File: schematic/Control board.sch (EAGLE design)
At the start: 14 parts, among them IC2 ATTINY44A

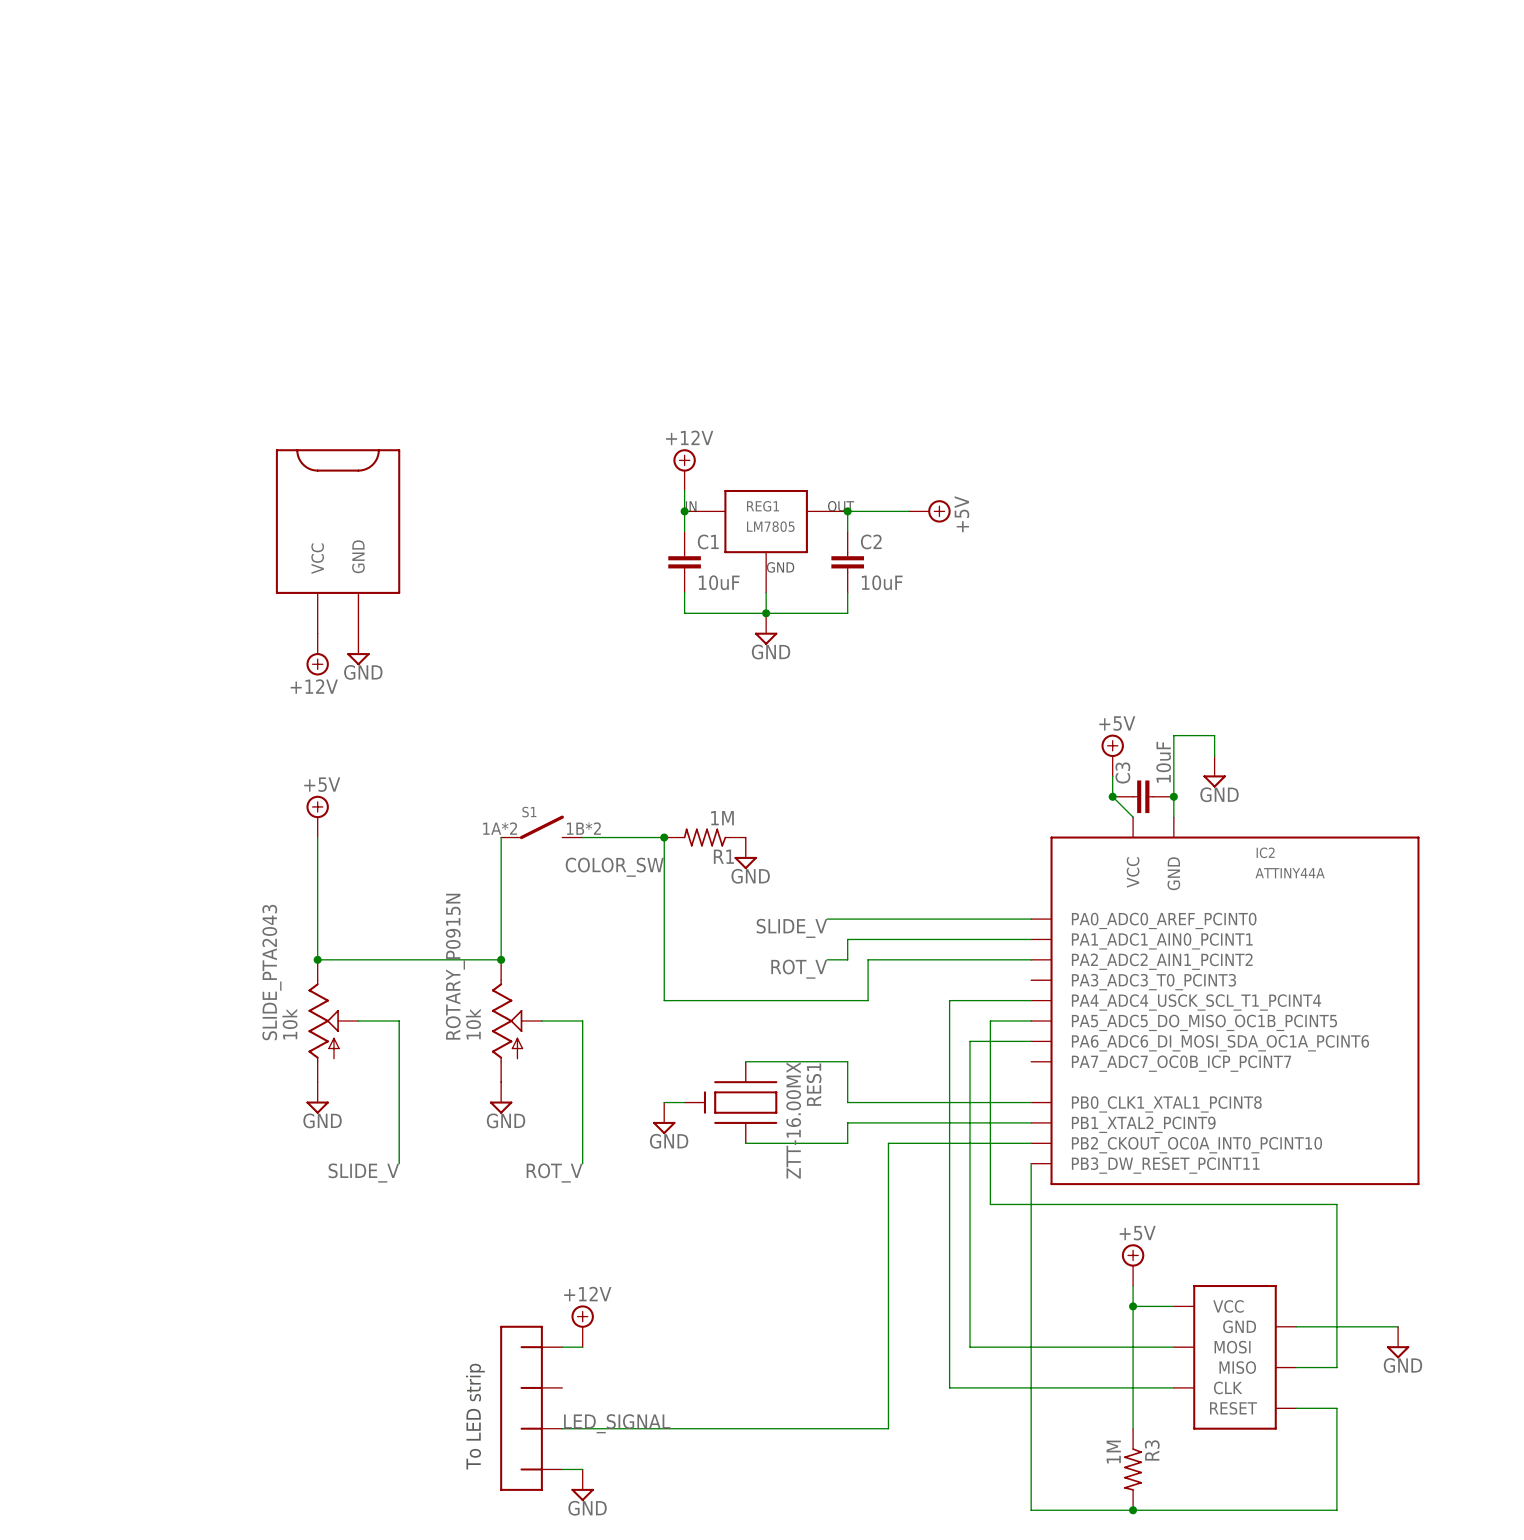
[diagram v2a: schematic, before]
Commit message: Voltage regulator and DIP microcontroller are too big, replacing with small SMD components
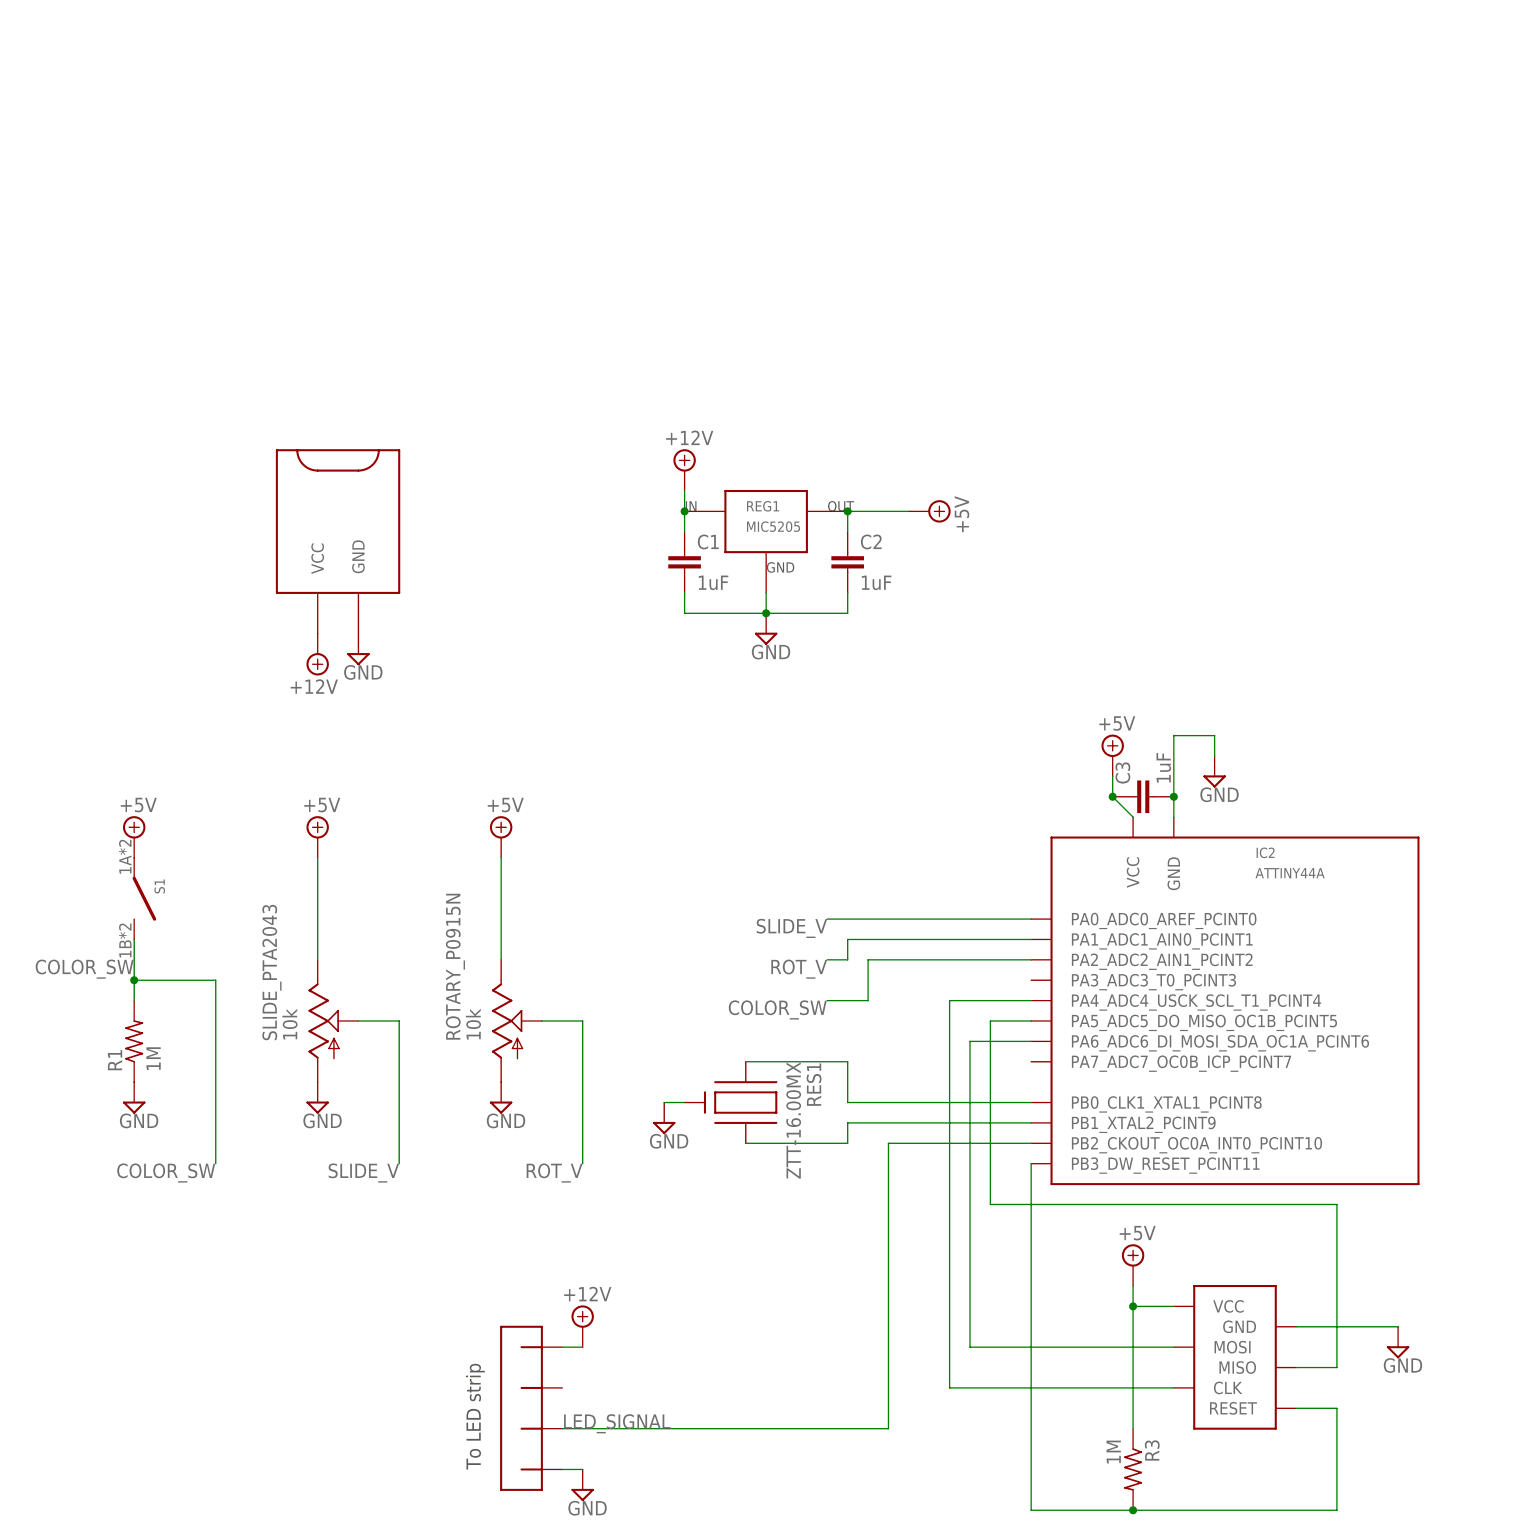
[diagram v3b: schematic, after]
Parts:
- C1, C2, C3: value 10uF -> 1uF
- REG1: value LM7805 -> MIC5205; device RGB LED project:LM7805 -> RGB LED project:MIC5205
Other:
- moved on the sheet: R1, S1
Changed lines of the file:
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@@
 <part name="SUPPLY4" library="supply2" deviceset="GND" device=""/>
 <part name="SUPPLY5" library="supply2" deviceset="+12V" device=""/>
-<part name="C1" library="resistor" deviceset="C-EU" device="C0603" value="10uF"/>
+<part name="C1" library="resistor" deviceset="C-EU" device="C0603" value="1uF"/>
 <part name="SUPPLY6" library="supply2" deviceset="GND" device=""/>
 <part name="SUPPLY8" library="supply2" deviceset="+5V" device=""/>
@@
 <part name="SUPPLY17" library="supply2" deviceset="GND" device=""/>
 <part name="CONN1" library="RGB LED project" deviceset="4-PIN-RIGHT-ANGLE" device=""/>
-<part name="REG1" library="RGB LED project" deviceset="LM7805" device="" value="LM7805"/>
-<part name="C2" library="resistor" deviceset="C-EU" device="C0603" value="10uF"/>
-<part name="C3" library="resistor" deviceset="C-EU" device="C0603" value="10uF"/>
+<part name="C2" library="resistor" deviceset="C-EU" device="C0603" value="1uF"/>
+<part name="C3" library="resistor" deviceset="C-EU" device="C0603" value="1uF"/>
+<part name="REG1" library="RGB LED project" deviceset="MIC5205" device=""/>
+<part name="SUPPLY7" library="supply2" deviceset="+5V" device=""/>
+<part name="SUPPLY18" library="supply2" deviceset="+5V" device=""/>
 </parts>
 <sheets>
@@
 </plain>
 <instances>
-<instance part="S1" gate="G$1" x="-35.56" y="-7.62"/>
+<instance part="S1" gate="G$1" x="-83.82" y="-12.7" rot="R270"/>
 <instance part="ROTARY_P0915N" gate="G$1" x="-38.1" y="-30.48"/>
 <instance part="SLIDE_PTA2043" gate="G$1" x="-60.96" y="-30.48"/>
-<instance part="SUPPLY1" gate="+5V" x="-60.96" y="-5.08"/>
+<instance part="SUPPLY1" gate="+5V" x="-60.96" y="-7.62"/>
 <instance part="SUPPLY2" gate="GND" x="-60.96" y="-40.64"/>
 <instance part="SUPPLY3" gate="GND" x="-38.1" y="-40.64"/>
-<instance part="R1" gate="G$1" x="-12.7" y="-7.62" rot="R180"/>
-<instance part="SUPPLY4" gate="GND" x="-7.62" y="-10.16"/>
+<instance part="R1" gate="G$1" x="-83.82" y="-33.02" rot="R90"/>
+<instance part="SUPPLY4" gate="GND" x="-83.82" y="-40.64"/>
 <instance part="SUPPLY5" gate="+12V" x="-15.24" y="38.1"/>
 <instance part="C1" gate="G$1" x="-15.24" y="27.94"/>
@@
 <instance part="SUPPLY17" gate="GND" x="-27.94" y="-88.9"/>
 <instance part="CONN1" gate="G$1" x="-35.56" y="-78.74" rot="R180"/>
-<instance part="REG1" gate="G$1" x="-5.08" y="33.02"/>
 <instance part="C2" gate="G$1" x="5.08" y="27.94"/>
 <instance part="C3" gate="G$1" x="40.64" y="-2.54" rot="R90"/>
+<instance part="REG1" gate="G$1" x="-5.08" y="33.02"/>
+<instance part="SUPPLY7" gate="+5V" x="-38.1" y="-7.62"/>
+<instance part="SUPPLY18" gate="+5V" x="-83.82" y="-7.62"/>
 </instances>
 <busses>
@@
 <pinref part="SUPPLY1" gate="+5V" pin="+5V"/>
 <pinref part="SLIDE_PTA2043" gate="G$1" pin="B"/>
-<wire x1="-60.96" y1="-7.62" x2="-60.96" y2="-22.86" width="0.1524" layer="91"/>
-<pinref part="ROTARY_P0915N" gate="G$1" pin="B"/>
-<wire x1="-60.96" y1="-22.86" x2="-38.1" y2="-22.86" width="0.1524" layer="91"/>
-<pinref part="S1" gate="G$1" pin="P$1"/>
-<wire x1="-38.1" y1="-22.86" x2="-38.1" y2="-7.62" width="0.1524" layer="91"/>
-<junction x="-60.96" y="-22.86"/>
-<junction x="-38.1" y="-22.86"/>
+<wire x1="-60.96" y1="-10.16" x2="-60.96" y2="-22.86" width="0.1524" layer="91"/>
 </segment>
 <segment>
 <wire x1="5.08" y1="33.02" x2="12.7" y2="33.02" width="0.1524" layer="91"/>
 <pinref part="SUPPLY8" gate="+5V" pin="+5V"/>
-<pinref part="REG1" gate="G$1" pin="OUT"/>
 <pinref part="C2" gate="G$1" pin="1"/>
 <wire x1="5.08" y1="30.48" x2="5.08" y2="33.02" width="0.1524" layer="91"/>
+<pinref part="REG1" gate="G$1" pin="OUT"/>
 <junction x="5.08" y="33.02"/>
 </segment>
@@
 <junction x="40.64" y="-66.04"/>
 </segment>
+<segment>
+<pinref part="S1" gate="G$1" pin="P$1"/>
+<pinref part="SUPPLY18" gate="+5V" pin="+5V"/>
+</segment>
+<segment>
+<pinref part="ROTARY_P0915N" gate="G$1" pin="B"/>
+<pinref part="SUPPLY7" gate="+5V" pin="+5V"/>
+<wire x1="-38.1" y1="-10.16" x2="-38.1" y2="-22.86" width="0.1524" layer="91"/>
+</segment>
 </net>
 <net name="SLIDE_V" class="0">
@@
 <net name="COLOR_SW" class="0">
 <segment>
-<pinref part="S1" gate="G$1" pin="P$2"/>
-<wire x1="-27.94" y1="-7.62" x2="-17.78" y2="-7.62" width="0.1524" layer="91"/>
-<wire x1="-17.78" y1="-7.62" x2="-17.78" y2="-27.94" width="0.1524" layer="91"/>
-<pinref part="R1" gate="G$1" pin="2"/>
-<junction x="-17.78" y="-7.62"/>
-<label x="-17.78" y="-10.16" size="1.778" layer="95" rot="R180"/>
+<label x="-83.82" y="-22.86" size="1.778" layer="95" rot="R180"/>
 <pinref part="IC2" gate="G$1" pin="PA2_ADC2_AIN1_PCINT2"/>
 <wire x1="27.94" y1="-22.86" x2="7.62" y2="-22.86" width="0.1524" layer="91"/>
 <wire x1="7.62" y1="-22.86" x2="7.62" y2="-27.94" width="0.1524" layer="91"/>
-<wire x1="7.62" y1="-27.94" x2="-17.78" y2="-27.94" width="0.1524" layer="91"/>
+<label x="2.54" y="-27.94" size="1.778" layer="95" rot="R180"/>
+<wire x1="7.62" y1="-27.94" x2="2.54" y2="-27.94" width="0.1524" layer="91"/>
+</segment>
+<segment>
+<pinref part="S1" gate="G$1" pin="P$2"/>
+<pinref part="R1" gate="G$1" pin="2"/>
+<wire x1="-83.82" y1="-27.94" x2="-83.82" y2="-25.4" width="0.1524" layer="91"/>
+<wire x1="-83.82" y1="-25.4" x2="-83.82" y2="-20.32" width="0.1524" layer="91"/>
+<wire x1="-83.82" y1="-25.4" x2="-73.66" y2="-25.4" width="0.1524" layer="91"/>
+<wire x1="-73.66" y1="-25.4" x2="-73.66" y2="-48.26" width="0.1524" layer="91"/>
+<junction x="-83.82" y="-25.4"/>
+<label x="-73.66" y="-48.26" size="1.778" layer="95" rot="R180"/>
 </segment>
 </net>
@@
 <pinref part="SUPPLY6" gate="GND" pin="GND"/>
 <junction x="-5.08" y="20.32"/>
-<pinref part="REG1" gate="G$1" pin="GND"/>
 <pinref part="C2" gate="G$1" pin="2"/>
 <wire x1="-5.08" y1="20.32" x2="5.08" y2="20.32" width="0.1524" layer="91"/>
 <wire x1="5.08" y1="20.32" x2="5.08" y2="22.86" width="0.1524" layer="91"/>
+<pinref part="REG1" gate="G$1" pin="GND"/>
 </segment>
 <segment>
@@
 <segment>
 <pinref part="SUPPLY5" gate="+12V" pin="+12V"/>
-<wire x1="-15.24" y1="35.56" x2="-15.24" y2="33.02" width="0.1524" layer="91"/>
 <pinref part="C1" gate="G$1" pin="1"/>
 <wire x1="-15.24" y1="30.48" x2="-15.24" y2="33.02" width="0.1524" layer="91"/>
+<pinref part="REG1" gate="G$1" pin="IN"/>
+<wire x1="-15.24" y1="33.02" x2="-15.24" y2="35.56" width="0.1524" layer="91"/>
 <junction x="-15.24" y="33.02"/>
-<pinref part="REG1" gate="G$1" pin="IN"/>
-</segment>
-<segment>
+</segment>
+<segment>

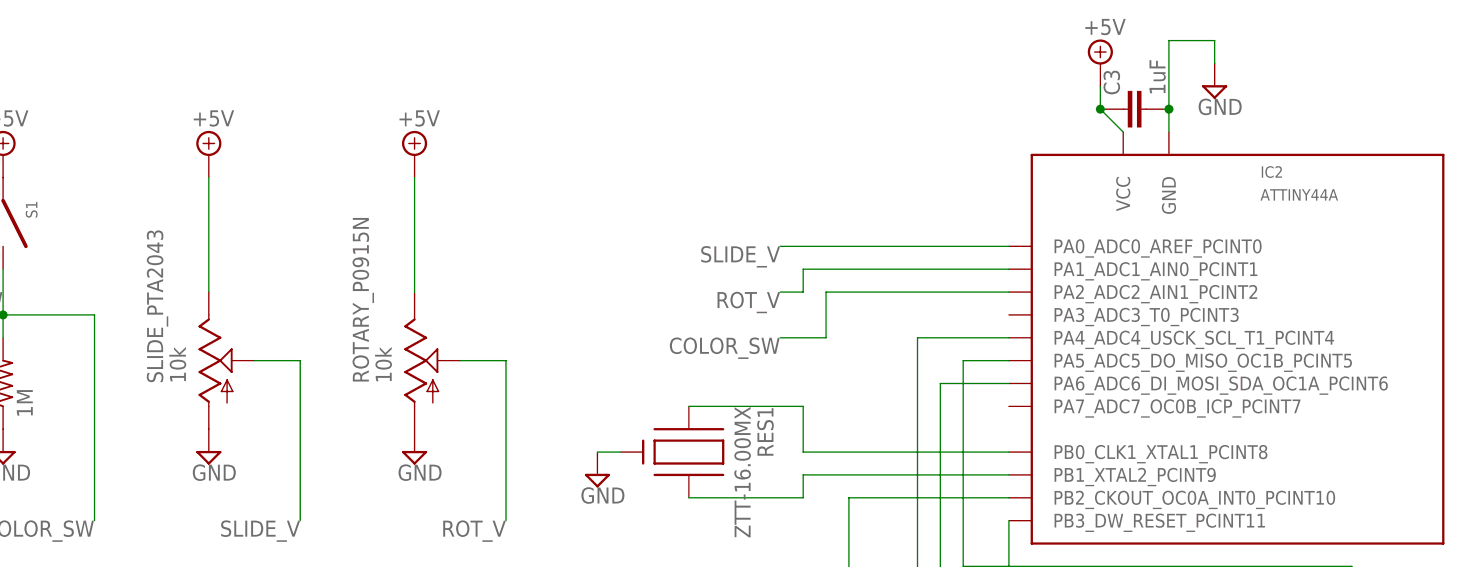
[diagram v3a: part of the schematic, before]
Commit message: Updated board with QFN-20 microcontroller
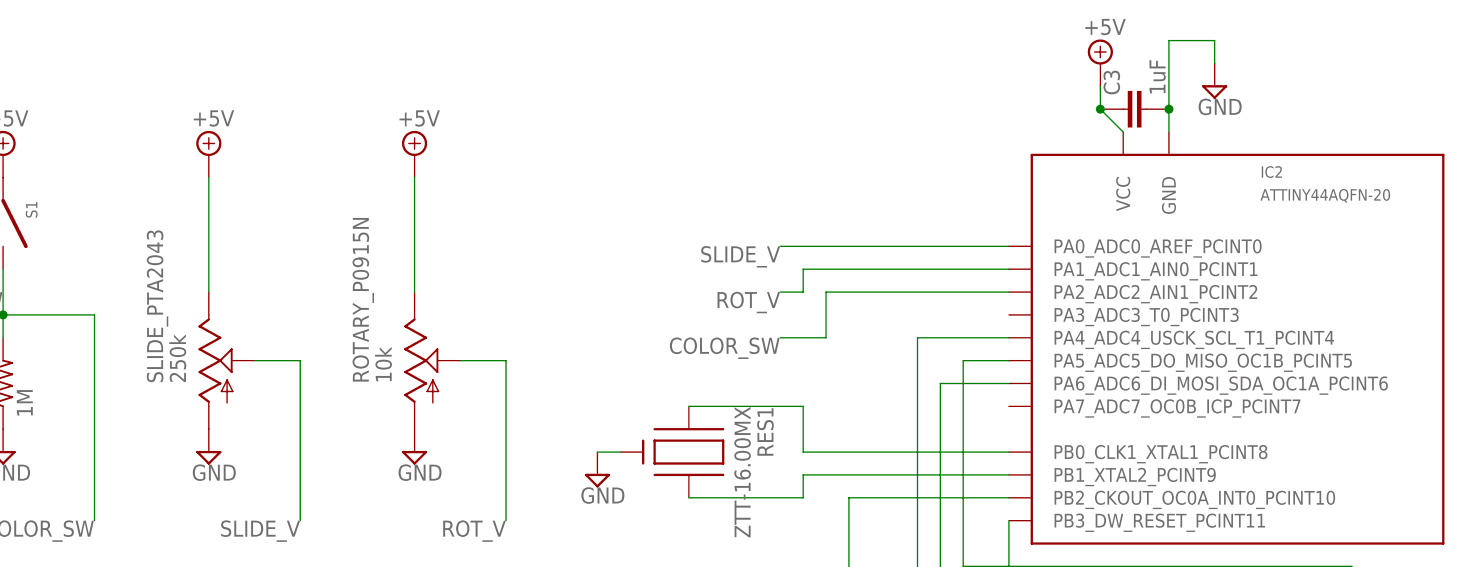
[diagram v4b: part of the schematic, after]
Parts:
- IC2: value ATTINY44A -> ATTINY44AQFN-20; device RGB LED project:ATTINY44A -> RGB LED project:ATTINY44AQFN-20
- SLIDE_PTA2043: value 10k -> 250k
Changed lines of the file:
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@@
 <part name="S1" library="RGB LED project" deviceset="D6R00" device=""/>
 <part name="ROTARY_P0915N" library="RGB LED project" deviceset="P0915N" device="" value="10k"/>
-<part name="SLIDE_PTA2043" library="RGB LED project" deviceset="PTA2043" device="" value="10k"/>
+<part name="SLIDE_PTA2043" library="RGB LED project" deviceset="PTA2043" device="" value="250k"/>
 <part name="SUPPLY1" library="supply2" deviceset="+5V" device=""/>
 <part name="SUPPLY2" library="supply2" deviceset="GND" device=""/>
@@
 <part name="SUPPLY9" library="supply2" deviceset="+12V" device=""/>
 <part name="SUPPLY10" library="supply2" deviceset="GND" device=""/>
-<part name="IC2" library="RGB LED project" deviceset="ATTINY44A" device=""/>
+<part name="IC2" library="RGB LED project" deviceset="ATTINY44A" device="QFN-20"/>
 <part name="SUPPLY11" library="supply2" deviceset="GND" device=""/>
 <part name="SUPPLY12" library="supply2" deviceset="+5V" device=""/>

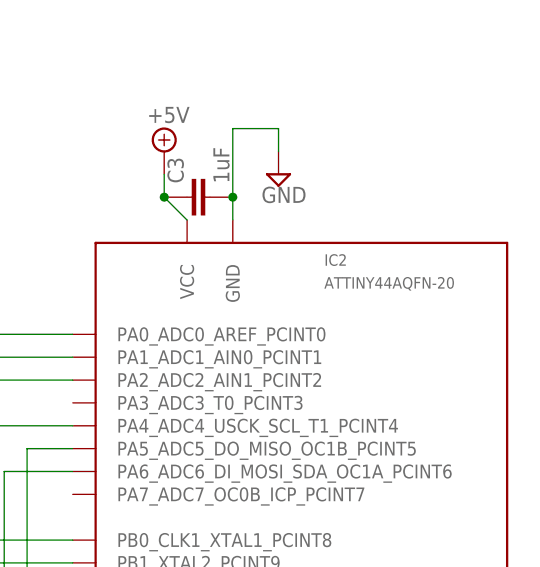
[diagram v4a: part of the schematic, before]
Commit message: Updated board with QFN-20 microcontroller
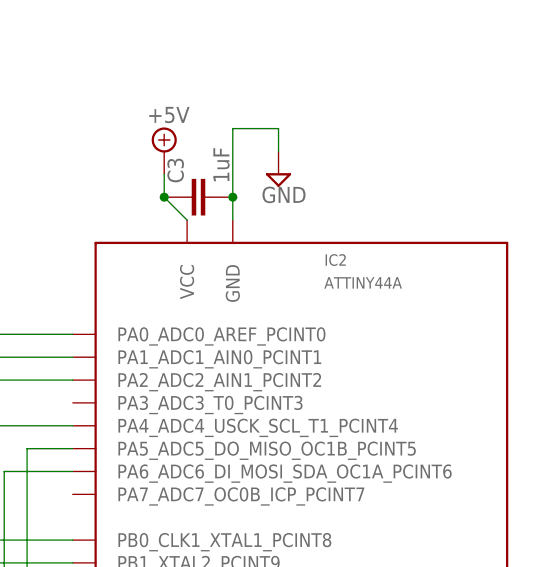
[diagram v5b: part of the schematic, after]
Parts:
- IC2: value ATTINY44AQFN-20 -> ATTINY44A
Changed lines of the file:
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@@
 <part name="SUPPLY9" library="supply2" deviceset="+12V" device=""/>
 <part name="SUPPLY10" library="supply2" deviceset="GND" device=""/>
-<part name="IC2" library="RGB LED project" deviceset="ATTINY44A" device="QFN-20"/>
+<part name="IC2" library="RGB LED project" deviceset="ATTINY44A" device="QFN-20" value="ATTINY44A"/>
 <part name="SUPPLY11" library="supply2" deviceset="GND" device=""/>
 <part name="SUPPLY12" library="supply2" deviceset="+5V" device=""/>
